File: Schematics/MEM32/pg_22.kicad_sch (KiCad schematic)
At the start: 4 parts, among them U1806 XLRULOGIC, U1901 F244, U1903 TSXXPAL, U2908 F64

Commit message: MEM32: eliminate half of MRUDR3, tested to 4.2s (rm125)
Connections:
- net B_HTLRU0: no longer U1901.3 (Y7)
- net B_HTLRU1: no longer U1901.5 (Y6)
- net B_HTLRU2: no longer U1901.7 (Y5)
- net B_HTLRU3: no longer U1901.9 (Y4)
- net BL_LRU0_HD: no longer names the net of U1806.47 (TMP16)
- net BL_LRU0_HD: no longer U1901.17 (I7)
- net BL_LRU1_HD: no longer names the net of U1806.48 (TMP17)
- net BL_LRU1_HD: no longer U1901.15 (I6)
- net BL_LRU2_HD: no longer names the net of U1806.49 (TMP18)
- net BL_LRU2_HD: no longer U1901.13 (I5)
- net BL_LRU3_HD: no longer names the net of U1806.50 (TMP19)
- net BL_LRU3_HD: no longer U1901.11 (I4)
- net LRU5_OE~: no longer names the net of U1806.26 (TMP2)
- net LRU5_OE~: no longer U1901.19 (OE1)
- no-connect marks 19 -> 33
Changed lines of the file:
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@@
     (comment 4 "RELEASED")
   )
-  (junction (at 307.34 325.12) (diameter 0) (color 0 0 0 0)
-  )
   (junction (at 276.86 218.44) (diameter 0) (color 0 0 0 0)
   )
   (junction (at 276.86 233.68) (diameter 0) (color 0 0 0 0)
   )
-  (junction (at 302.26 320.04) (diameter 0) (color 0 0 0 0)
-  )
-  (junction (at 317.5 335.28) (diameter 0) (color 0 0 0 0)
-  )
   (junction (at 109.22 86.36) (diameter 0) (color 0 0 0 0)
   )
   (junction (at 271.78 271.78) (diameter 0) (color 0 0 0 0)
-  )
-  (junction (at 312.42 330.2) (diameter 0) (color 0 0 0 0)
   )
   (junction (at 276.86 228.6) (diameter 0) (color 0 0 0 0)
@@
   (no_connect (at 152.4 71.12))
   (no_connect (at 66.04 274.32))
+  (no_connect (at 264.16 345.44))
   (no_connect (at 127 269.24))
   (no_connect (at 127 254))
+  (no_connect (at 127 309.88))
   (no_connect (at 127 264.16))
   (no_connect (at 127 314.96))
   (no_connect (at 127 274.32))
+  (no_connect (at 297.18 345.44))
+  (no_connect (at 127 304.8))
   (no_connect (at 127 228.6))
+  (no_connect (at 127 294.64))
   (no_connect (at 127 233.68))
   (no_connect (at 127 284.48))
   (no_connect (at 127 248.92))
+  (no_connect (at 297.18 355.6))
+  (no_connect (at 297.18 340.36))
+  (no_connect (at 127 223.52))
   (no_connect (at 127 289.56))
+  (no_connect (at 127 299.72))
   (no_connect (at 279.4 246.38))
   (no_connect (at 127 238.76))
+  (no_connect (at 284.48 304.8))
+  (no_connect (at 264.16 355.6))
   (no_connect (at 127 320.04))
   (no_connect (at 127 243.84))
   (no_connect (at 127 279.4))
+  (no_connect (at 264.16 350.52))
   (no_connect (at 127 213.36))
   (no_connect (at 127 259.08))
+  (no_connect (at 297.18 350.52))
+  (no_connect (at 264.16 340.36))
   (bus_entry (at 68.58 63.5) (size 2.54 2.54)
     (stroke (width 0) (type default))
@@
     (stroke (width 0) (type default))
   )
-  (wire (pts (xy 297.18 325.12) (xy 307.34 325.12))
+  (wire (pts (xy 297.18 325.12) (xy 345.44 325.12))
     (stroke (width 0) (type default))
   )
@@
     (stroke (width 0) (type default))
   )
-  (wire (pts (xy 297.18 355.6) (xy 317.5 355.6))
-    (stroke (width 0) (type default))
-  )
   (wire (pts (xy 266.7 261.62) (xy 279.4 261.62))
     (stroke (width 0) (type default))
@@
     (stroke (width 0) (type default))
   )
-  (wire (pts (xy 256.54 297.18) (xy 284.48 297.18))
-    (stroke (width 0) (type default))
-  )
-  (wire (pts (xy 127 304.8) (xy 157.48 304.8))
-    (stroke (width 0) (type default))
-  )
   (wire (pts (xy 35.56 162.56) (xy 66.04 162.56))
     (stroke (width 0) (type default))
   )
-  (wire (pts (xy 127 299.72) (xy 157.48 299.72))
-    (stroke (width 0) (type default))
-  )
-  (wire (pts (xy 297.18 340.36) (xy 302.26 340.36))
-    (stroke (width 0) (type default))
-  )
   (wire (pts (xy 152.4 55.88) (xy 187.96 55.88))
     (stroke (width 0) (type default))
@@
     (stroke (width 0) (type default))
   )
-  (wire (pts (xy 297.18 345.44) (xy 307.34 345.44))
-    (stroke (width 0) (type default))
-  )
   (wire (pts (xy 60.96 213.36) (xy 66.04 213.36))
     (stroke (width 0) (type default))
@@
     (stroke (width 0) (type default))
   )
-  (wire (pts (xy 297.18 335.28) (xy 317.5 335.28))
-    (stroke (width 0) (type default))
-  )
   (bus (pts (xy 190.5 88.9) (xy 190.5 93.98))
     (stroke (width 0) (type default))
@@
     (stroke (width 0) (type default))
   )
-  (wire (pts (xy 297.18 350.52) (xy 312.42 350.52))
-    (stroke (width 0) (type default))
-  )
-  (wire (pts (xy 302.26 320.04) (xy 345.44 320.04))
+  (wire (pts (xy 297.18 320.04) (xy 345.44 320.04))
     (stroke (width 0) (type default))
   )
@@
     (stroke (width 0) (type default))
   )
-  (wire (pts (xy 307.34 345.44) (xy 307.34 325.12))
-    (stroke (width 0) (type default))
-  )
   (wire (pts (xy 185.42 76.2) (xy 152.4 76.2))
     (stroke (width 0) (type default))
@@
     (stroke (width 0) (type default))
   )
-  (wire (pts (xy 317.5 335.28) (xy 345.44 335.28))
+  (wire (pts (xy 297.18 335.28) (xy 345.44 335.28))
     (stroke (width 0) (type default))
   )
@@
     (stroke (width 0) (type default))
   )
-  (wire (pts (xy 233.68 340.36) (xy 264.16 340.36))
-    (stroke (width 0) (type default))
-  )
   (wire (pts (xy 152.4 96.52) (xy 187.96 96.52))
     (stroke (width 0) (type default))
@@
     (stroke (width 0) (type default))
   )
-  (wire (pts (xy 127 294.64) (xy 157.48 294.64))
-    (stroke (width 0) (type default))
-  )
   (wire (pts (xy 60.96 223.52) (xy 66.04 223.52))
     (stroke (width 0) (type default))
@@
     (stroke (width 0) (type default))
   )
-  (wire (pts (xy 127 223.52) (xy 157.48 223.52))
-    (stroke (width 0) (type default))
-  )
   (wire (pts (xy 60.96 193.04) (xy 66.04 193.04))
     (stroke (width 0) (type default))
@@
     (stroke (width 0) (type default))
   )
-  (wire (pts (xy 233.68 345.44) (xy 264.16 345.44))
-    (stroke (width 0) (type default))
-  )
   (wire (pts (xy 60.96 248.92) (xy 66.04 248.92))
     (stroke (width 0) (type default))
@@
     (stroke (width 0) (type default))
   )
-  (wire (pts (xy 284.48 297.18) (xy 284.48 304.8))
-    (stroke (width 0) (type default))
-  )
   (wire (pts (xy 127 335.28) (xy 157.48 335.28))
     (stroke (width 0) (type default))
@@
     (stroke (width 0) (type default))
   )
-  (wire (pts (xy 127 309.88) (xy 157.48 309.88))
-    (stroke (width 0) (type default))
-  )
   (wire (pts (xy 127 203.2) (xy 132.08 203.2))
     (stroke (width 0) (type default))
@@
     (stroke (width 0) (type default))
   )
-  (wire (pts (xy 302.26 340.36) (xy 302.26 320.04))
-    (stroke (width 0) (type default))
-  )
   (bus (pts (xy 157.48 185.42) (xy 157.48 190.5))
     (stroke (width 0) (type default))
@@
     (stroke (width 0) (type default))
   )
-  (wire (pts (xy 312.42 330.2) (xy 345.44 330.2))
-    (stroke (width 0) (type default))
-  )
   (wire (pts (xy 71.12 81.28) (xy 114.3 81.28))
     (stroke (width 0) (type default))
   )
-  (wire (pts (xy 297.18 330.2) (xy 312.42 330.2))
-    (stroke (width 0) (type default))
-  )
-  (wire (pts (xy 297.18 320.04) (xy 302.26 320.04))
-    (stroke (width 0) (type default))
-  )
-  (wire (pts (xy 317.5 355.6) (xy 317.5 335.28))
-    (stroke (width 0) (type default))
-  )
-  (wire (pts (xy 312.42 350.52) (xy 312.42 330.2))
+  (wire (pts (xy 297.18 330.2) (xy 345.44 330.2))
     (stroke (width 0) (type default))
   )
@@
     (stroke (width 0) (type default))
   )
-  (wire (pts (xy 233.68 350.52) (xy 264.16 350.52))
-    (stroke (width 0) (type default))
-  )
-  (wire (pts (xy 233.68 355.6) (xy 264.16 355.6))
-    (stroke (width 0) (type default))
-  )
   (wire (pts (xy 127 147.32) (xy 154.94 147.32))
     (stroke (width 0) (type default))
@@
     (stroke (width 0) (type default))
   )
-  (wire (pts (xy 307.34 325.12) (xy 345.44 325.12))
-    (stroke (width 0) (type default))
-  )
   (wire (pts (xy 271.78 271.78) (xy 271.78 251.46))
     (stroke (width 0) (type default))
@@
     (stroke (width 0) (type default))
   )
-  (label "BL_LRU3_HD" (at 132.08 309.88 0) (fields_autoplaced)
-    (effects (font (size 2.54 2.54)) (justify left bottom))
-  )
   (label "B_HTLRU2" (at 322.58 325.12 0) (fields_autoplaced)
     (effects (font (size 2.54 2.54)) (justify left bottom))
@@
     (effects (font (size 2.54 2.54)) (justify left bottom))
   )
-  (label "BL_LRU0_HD" (at 132.08 294.64 0) (fields_autoplaced)
-    (effects (font (size 2.54 2.54)) (justify left bottom))
-  )
   (label "TAGBL_54" (at 81.28 66.04 0) (fields_autoplaced)
     (effects (font (size 2.54 2.54)) (justify left bottom))
@@
     (effects (font (size 2.54 2.54)) (justify left bottom))
   )
-  (label "LRU5_OE~" (at 256.54 297.18 0) (fields_autoplaced)
-    (effects (font (size 2.54 2.54)) (justify left bottom))
-  )
   (label "TAGBL_49" (at 132.08 137.16 0) (fields_autoplaced)
     (effects (font (size 2.54 2.54)) (justify left bottom))
@@
     (effects (font (size 2.54 2.54)) (justify left bottom))
   )
-  (label "BL_LRU1_HD" (at 132.08 299.72 0) (fields_autoplaced)
-    (effects (font (size 2.54 2.54)) (justify left bottom))
-  )
   (label "BL_LRU2_QD" (at 132.08 335.28 0) (fields_autoplaced)
     (effects (font (size 2.54 2.54)) (justify left bottom))
   )
-  (label "BL_LRU3_HD" (at 233.68 340.36 0) (fields_autoplaced)
-    (effects (font (size 2.54 2.54)) (justify left bottom))
-  )
   (label "COMMAND0" (at 160.02 96.52 0) (fields_autoplaced)
     (effects (font (size 2.54 2.54)) (justify left bottom))
@@
     (effects (font (size 2.54 2.54)) (justify left bottom))
   )
-  (label "BL_LRU1_HD" (at 233.68 350.52 0) (fields_autoplaced)
-    (effects (font (size 2.54 2.54)) (justify left bottom))
-  )
   (label "HITQ_BL" (at 35.56 142.24 0) (fields_autoplaced)
     (effects (font (size 2.54 2.54)) (justify left bottom))
@@
     (effects (font (size 2.54 2.54)) (justify left bottom))
   )
-  (label "BL_LRU0_HD" (at 233.68 355.6 0) (fields_autoplaced)
-    (effects (font (size 2.54 2.54)) (justify left bottom))
-  )
   (label "B_HTLRU2" (at 132.08 182.88 0) (fields_autoplaced)
     (effects (font (size 2.54 2.54)) (justify left bottom))
@@
     (effects (font (size 2.54 2.54)) (justify left bottom))
   )
-  (label "BL_LRU2_HD" (at 233.68 345.44 0) (fields_autoplaced)
-    (effects (font (size 2.54 2.54)) (justify left bottom))
-  )
-  (label "LRU5_OE~" (at 132.08 223.52 0) (fields_autoplaced)
-    (effects (font (size 2.54 2.54)) (justify left bottom))
-  )
   (label "BL_LPAR_QD" (at 35.56 172.72 0) (fields_autoplaced)
     (effects (font (size 2.54 2.54)) (justify left bottom))
@@
     (effects (font (size 2.54 2.54)) (justify left bottom))
   )
-  (label "BL_LRU2_HD" (at 132.08 304.8 0) (fields_autoplaced)
-    (effects (font (size 2.54 2.54)) (justify left bottom))
-  )

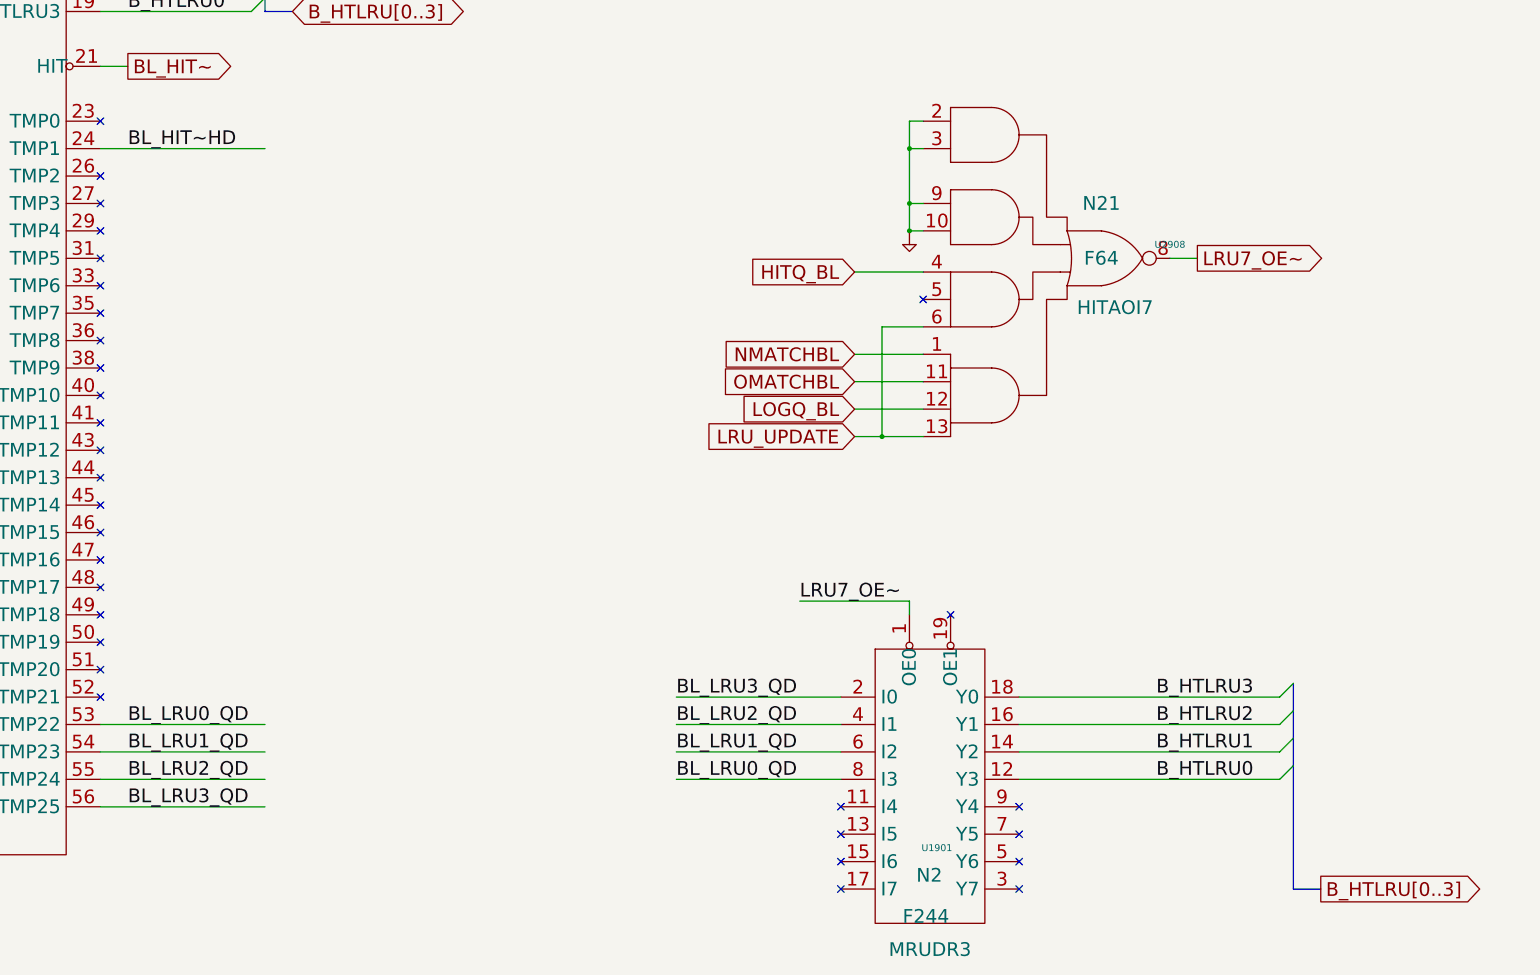
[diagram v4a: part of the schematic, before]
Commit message: MEM32: eliminate MRUDR3, tested to 4.1 (rm126)
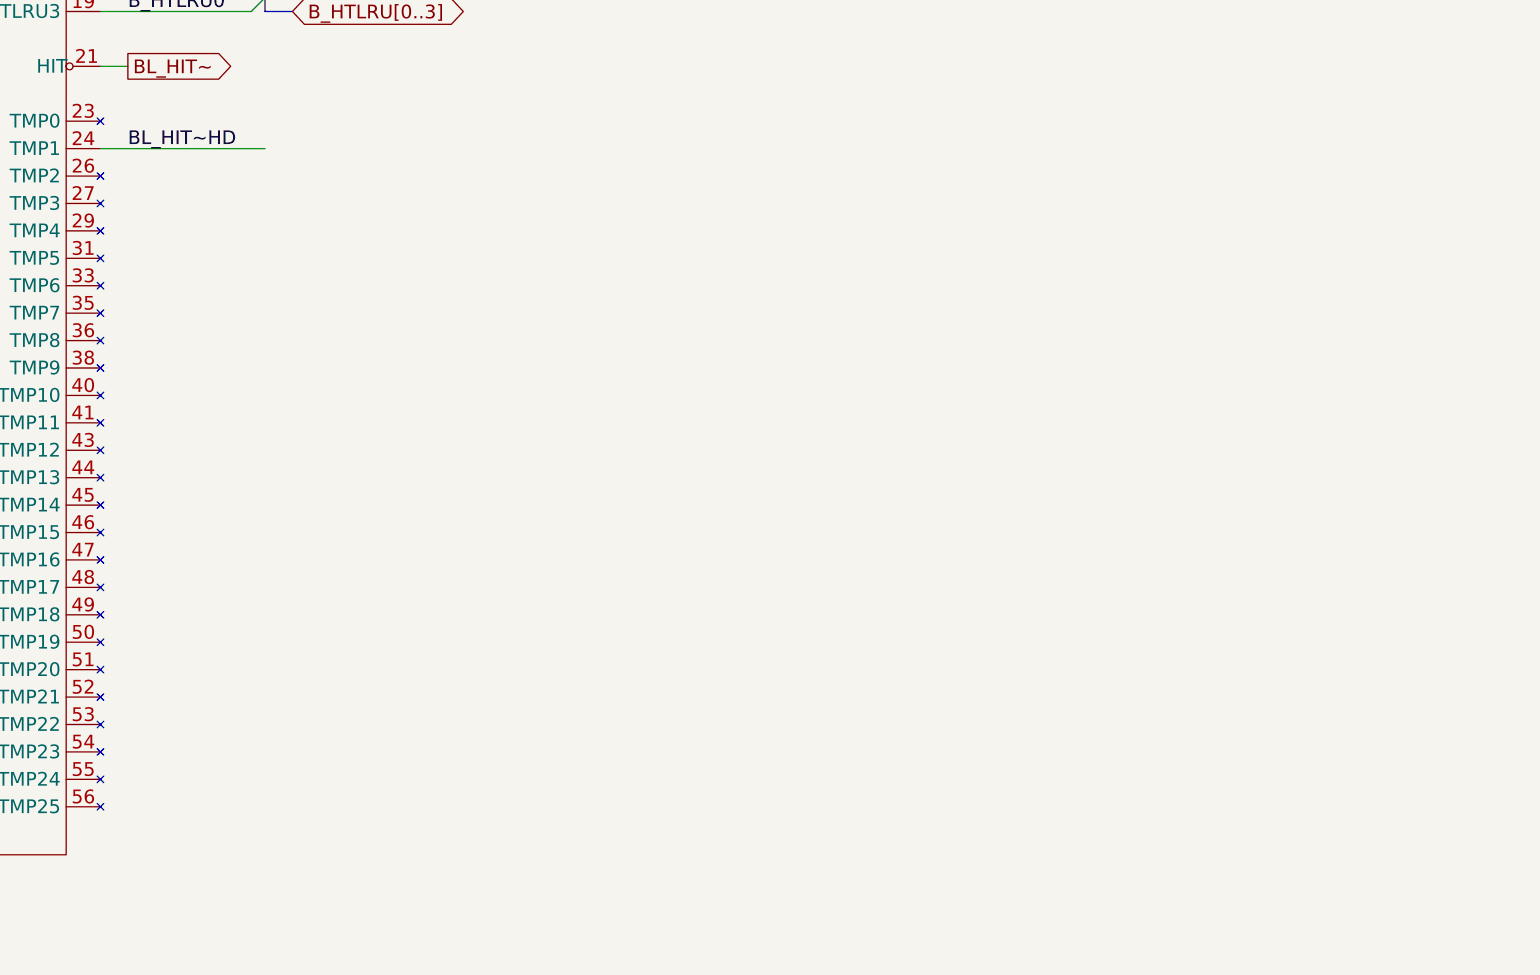
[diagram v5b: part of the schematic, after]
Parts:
- removed U1901: F244, symbol r1000:F244
- removed U2908: F64, symbol r1000:F64
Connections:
- net BL_LRU0_QD: no longer names the net of U1806.53 (TMP22)
- net BL_LRU1_QD: no longer names the net of U1806.54 (TMP23)
- net BL_LRU2_QD: no longer names the net of U1806.55 (TMP24)
- net BL_LRU3_QD: no longer names the net of U1806.56 (TMP25)
- no-connect marks 33 -> 27
